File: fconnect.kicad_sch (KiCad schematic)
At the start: 201 parts, among them J1 9001-11961C00A, J2 9001-11961C00A, J3 7760, J4 7760

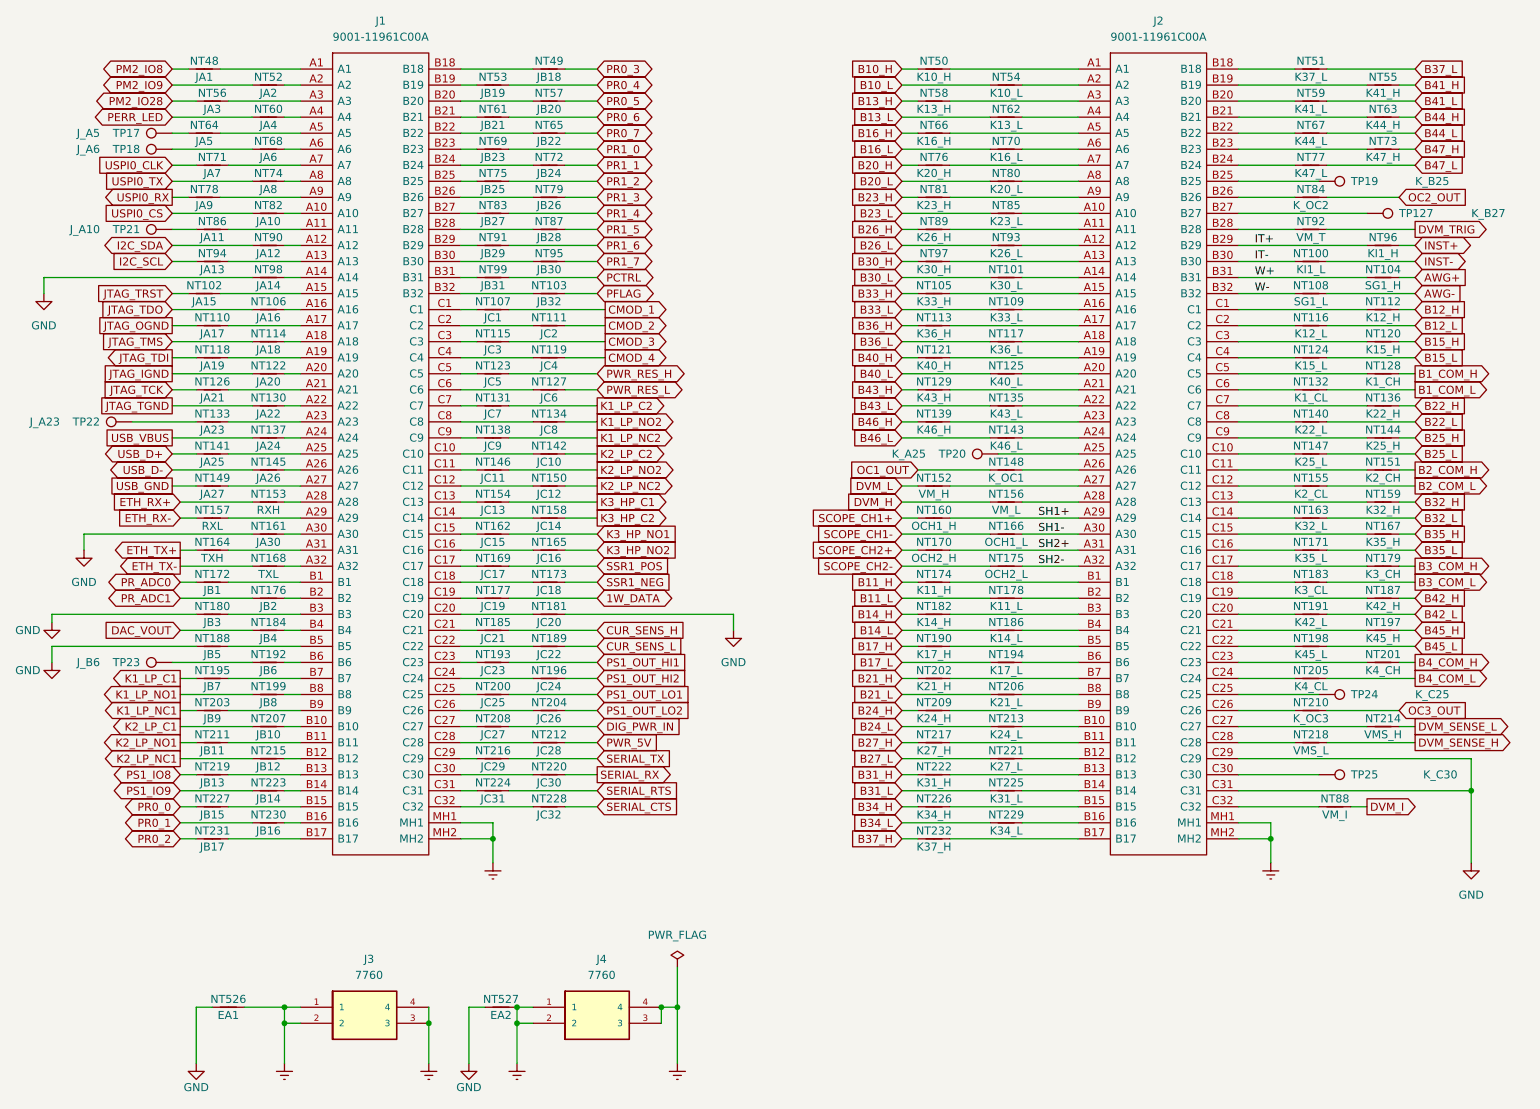
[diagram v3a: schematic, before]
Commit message: PCB Completed
PCB completed but final verification not completed
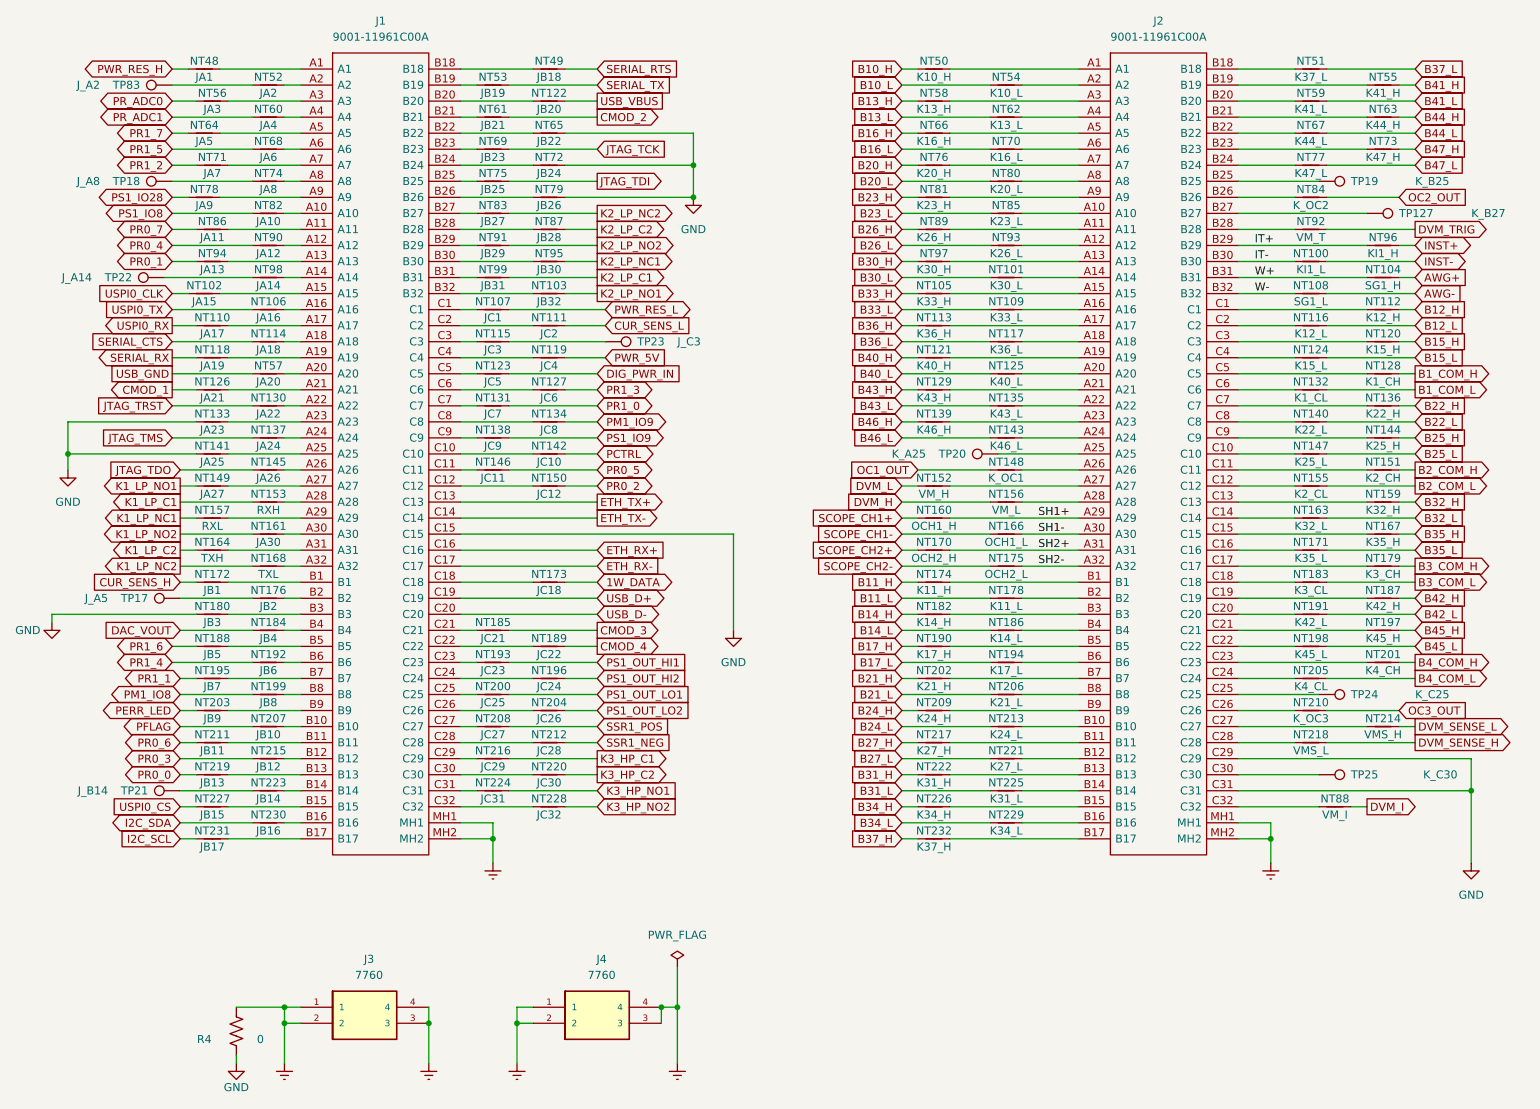
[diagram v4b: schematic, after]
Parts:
- removed NT154: JC13, NetTie:NetTie-2_Front1.0mm, symbol Device:NetTie_2
- removed NT158: JC14, NetTie:NetTie-2_Front1.0mm, symbol Device:NetTie_2
- removed NT162: JC15, NetTie:NetTie-2_Front1.0mm, symbol Device:NetTie_2
- removed NT165: JC16, NetTie:NetTie-2_Front1.0mm, symbol Device:NetTie_2
- removed NT169: JC17, NetTie:NetTie-2_Front1.0mm, symbol Device:NetTie_2
- removed NT177: JC19, NetTie:NetTie-2_Front1.0mm, symbol Device:NetTie_2
- removed NT181: JC20, NetTie:NetTie-2_Front1.0mm, symbol Device:NetTie_2
- removed NT526: EA1, NetTie:NetTie-2_Front1.0mm, symbol Device:NetTie_2
- removed NT527: EA2, NetTie:NetTie-2_Front1.0mm, symbol Device:NetTie_2
- added R4: 0, Resistor_THT:R_Axial_DIN0309_L9.0mm_D3.2mm_P12.70mm_Horizontal, symbol Device:R_US
- added TP83: J_A2, TestPoint:TestPoint_THTPad_D1.5mm_Drill0.7mm, symbol Connector:TestPoint
- NT122: value JA20 -> JB20
- NT57: value JB20 -> JA20
- TP17: footprint Connector_Pin:Pin_D0.9mm_L10.0mm_W2.4mm_FlatFork -> TestPoint:TestPoint_THTPad_D1.5mm_Drill0.7mm
- TP18: value J_A6 -> J_A8; footprint Connector_Pin:Pin_D0.9mm_L10.0mm_W2.4mm_FlatFork -> TestPoint:TestPoint_THTPad_D1.5mm_Drill0.7mm
- TP21: value J_A10 -> J_B14; footprint Connector_Pin:Pin_D0.9mm_L10.0mm_W2.4mm_FlatFork -> TestPoint:TestPoint_THTPad_D1.5mm_Drill0.7mm
- TP22: value J_A23 -> J_A14; footprint Connector_Pin:Pin_D0.9mm_L10.0mm_W2.4mm_FlatFork -> TestPoint:TestPoint_THTPad_D1.5mm_Drill0.7mm
- TP23: value J_B6 -> J_C3; footprint Connector_Pin:Pin_D0.9mm_L10.0mm_W2.4mm_FlatFork -> TestPoint:TestPoint_THTPad_D1.5mm_Drill0.7mm
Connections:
- net JTAG_IGND is gone; now on net USB_VBUS: NT122.1
- net JTAG_OGND is gone; now on net USPI0_RX: NT110.1
- net JTAG_TGND is gone; now on net JTAG_TRST: NT130.1
- net PM2_IO28 is gone; now on net PR_ADC0: NT56.1
- net PM2_IO8 is gone; now on net PWR_RES_H: NT48.1
- net 1W_DATA: now also NT173.1
- net CMOD_1: now also NT126.1; no longer NT107.1
- net CMOD_2: now also NT61.1; no longer NT111.1
- net CMOD_3: now also NT185.1; no longer NT115.1
- net CMOD_4: now also NT189.1; no longer NT119.1
- net CUR_SENS_H: now also NT172.1; no longer NT185.1
- net CUR_SENS_L: now also NT111.1; no longer NT189.1
- net DIG_PWR_IN: now also NT123.1; no longer NT208.1
- net ETH_RX+: now also J1.C16; no longer NT153.1
- net ETH_RX-: now also J1.C17; no longer NT157.1
- net ETH_TX+: now also J1.C13; no longer NT164.1
- net ETH_TX-: now also J1.C14; no longer NT168.1
- net Earth: now also R4.2
- net GND: now also J1.C15, NT133.1, NT141.1, NT65.1, NT72.1, NT79.1, R4.1; no longer NT161.1, NT188.1, NT98.1
- net I2C_SCL: now also NT231.1; no longer NT94.1
- net I2C_SDA: now also NT230.1; no longer NT90.1
- net JTAG_TCK: now also NT69.1; no longer NT126.1
- net JTAG_TDI: now also NT75.1; no longer NT118.1
- net JTAG_TDO: now also NT145.1; no longer NT106.1
- net JTAG_TMS: now also NT137.1; no longer NT114.1
- net JTAG_TRST: no longer NT102.1
- net K1_LP_C1: now also NT153.1; no longer NT195.1
- net K1_LP_C2: now also NT164.1; no longer NT131.1
- net K1_LP_NC1: now also NT157.1; no longer NT203.1
- net K1_LP_NC2: now also NT168.1; no longer NT138.1
- net K1_LP_NO1: now also NT149.1; no longer NT199.1
- net K1_LP_NO2: now also NT161.1; no longer NT134.1
- net K2_LP_C1: now also NT99.1; no longer NT207.1
- net K2_LP_C2: now also NT87.1; no longer NT142.1
- net K2_LP_NC1: now also NT95.1; no longer NT215.1
- net K2_LP_NC2: now also NT83.1; no longer NT150.1
- net K2_LP_NO1: now also NT103.1; no longer NT211.1
- net K2_LP_NO2: now also NT91.1; no longer NT146.1
- net K3_HP_C1: now also NT216.1
- net K3_HP_C2: now also NT220.1
- net K3_HP_NO1: now also NT224.1
- net K3_HP_NO2: now also NT228.1
- net PCTRL: now also NT142.1; no longer NT99.1
- net PERR_LED: now also NT203.1; no longer NT60.1
- net PFLAG: now also NT207.1; no longer NT103.1
- net PR0_0: now also NT219.1; no longer NT227.1
- net PR0_1: now also NT94.1; no longer NT230.1
- net PR0_2: now also NT150.1; no longer NT231.1
- net PR0_3: now also NT215.1; no longer NT49.1
- net PR0_4: now also NT90.1; no longer NT53.1
- net PR0_5: now also NT146.1; no longer NT57.1
- net PR0_6: now also NT211.1; no longer NT61.1
- net PR0_7: now also NT86.1; no longer NT65.1
- net PR1_0: now also NT131.1; no longer NT69.1
- net PR1_1: now also NT195.1; no longer NT72.1
- net PR1_2: now also NT71.1; no longer NT75.1
- net PR1_3: now also NT127.1; no longer NT79.1
- net PR1_4: now also NT192.1; no longer NT83.1
- net PR1_5: now also NT68.1; no longer NT87.1
- net PR1_6: now also NT188.1; no longer NT91.1
- net PR1_7: now also NT64.1; no longer NT95.1
- net PR_ADC0: no longer NT172.1
- net PR_ADC1: now also NT60.1; no longer NT176.1
- net PS1_IO8: now also NT82.1; no longer NT219.1
- net PS1_IO9: now also NT138.1; no longer NT223.1
- net PWR_5V: now also NT119.1; no longer NT212.1
- net PWR_RES_H: no longer NT123.1
- net PWR_RES_L: now also NT107.1; no longer NT127.1
- net SERIAL_CTS: now also NT114.1; no longer NT228.1
- net SERIAL_RTS: now also NT49.1; no longer NT224.1
- net SERIAL_RX: now also NT118.1; no longer NT220.1
- net SERIAL_TX: now also NT53.1; no longer NT216.1
- net SSR1_NEG: now also NT212.1; no longer NT173.1
- net SSR1_POS: now also NT208.1
- net USB_D+: now also J1.C19; no longer NT141.1
- net USB_D-: now also J1.C20; no longer NT145.1
- net USB_GND: now also NT57.1; no longer NT149.1
- net USB_VBUS: no longer NT137.1
- net USPI0_CLK: now also NT102.1; no longer NT71.1
- net USPI0_CS: now also NT227.1; no longer NT82.1
- net USPI0_RX: no longer NT78.1
- net USPI0_TX: now also NT106.1; no longer NT74.1
- net at TP21.1: now also NT223.1; no longer NT86.1
- net at TP17.1: now also NT176.1; no longer NT64.1
- net at TP22.1: now also NT98.1; no longer NT133.1
- net at TP18.1: now also NT74.1; no longer NT68.1
- net at NT122.2: now also J1.B20; no longer J1.A20
- net at NT57.2: now also J1.A20; no longer J1.B20
- net at TP23.1: now also NT115.1; no longer NT192.1
- net PM2_IO9: no longer names the net of NT52.1
- net PM2_IO9: now also TP83.1
- new net PM1_IO8: NT199.1
- new net PM1_IO9: NT134.1
- new net PS1_IO28: NT78.1
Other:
- moved on the sheet: TP21, TP22

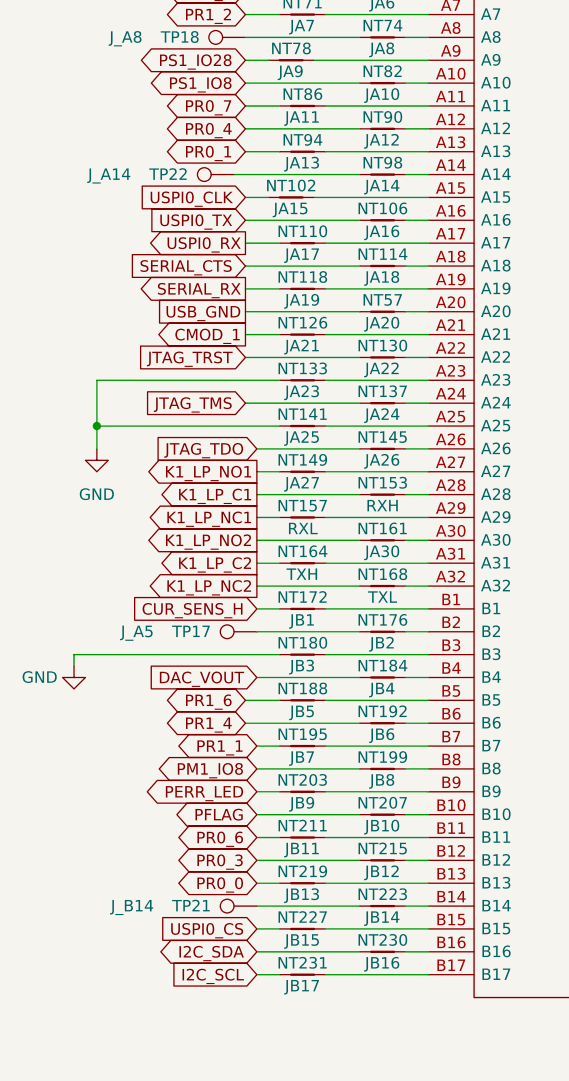
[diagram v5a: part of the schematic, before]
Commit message: Change custom connector
Use 8 pins to replace 6 pins
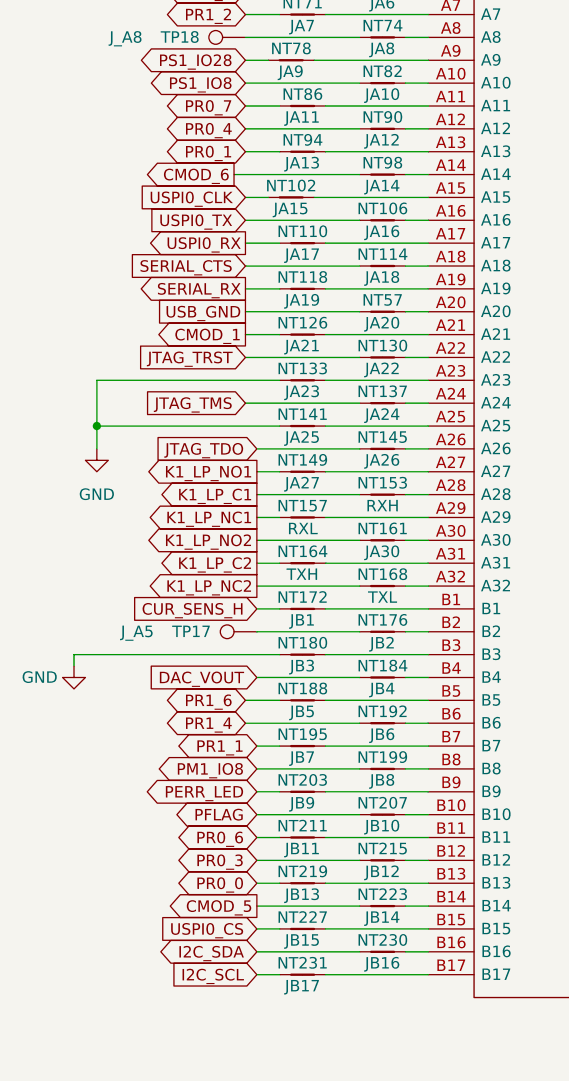
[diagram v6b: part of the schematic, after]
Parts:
- removed TP21: J_B14, TestPoint:TestPoint_THTPad_D1.5mm_Drill0.7mm, symbol Connector:TestPoint
- removed TP22: J_A14, TestPoint:TestPoint_THTPad_D1.5mm_Drill0.7mm, symbol Connector:TestPoint
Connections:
- net CMOD_5: now reaches NT223.1
- net CMOD_6: now reaches NT98.1
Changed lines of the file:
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@@
+    )
+  )
+  (global_label "CMOD_6" (shape output) (at 43.18 69.85 180) (fields_autoplaced)
+    (effects (font (size 1.27 1.27)) (justify right))
+    (property "Intersheet References" "${INTERSHEET_REFS}" (id 0) (at 33.2679 69.7706 0)
+      (effects (font (size 1.27 1.27)) (justify right) hide)
     )
   )
@@
     (property "Intersheet References" "${INTERSHEET_REFS}" (id 0) (at 249.5793 57.0706 0)
       (effects (font (size 1.27 1.27)) (justify left) hide)
+    )
+  )
+  (global_label "CMOD_5" (shape output) (at 45.72 151.13 180) (fields_autoplaced)
+    (effects (font (size 1.27 1.27)) (justify right))
+    (property "Intersheet References" "${INTERSHEET_REFS}" (id 0) (at 35.8079 151.0506 0)
+      (effects (font (size 1.27 1.27)) (justify right) hide)
     )
   )
@@
     (pin "2")
   )
-  (symbol (lib_id "Connector:TestPoint") (at 45.72 151.13 90) (mirror x) (unit 1)
-    (in_bom yes) (on_board yes)
-    (property "Reference" "TP21" (id 0) (at 40.64 151.13 90)
-      (effects (font (size 1.27 1.27)) (justify left))
-    )
-    (property "Value" "J_B14" (id 1) (at 34.29 151.13 90)
-      (effects (font (size 1.27 1.27)) (justify left))
-    )
-    (property "Footprint" "TestPoint:TestPoint_THTPad_D1.5mm_Drill0.7mm" (id 2) (at 45.72 156.21 0)
-      (effects (font (size 1.27 1.27)) hide)
-    )
-    (property "Datasheet" "~" (id 3) (at 45.72 156.21 0)
-      (effects (font (size 1.27 1.27)) hide)
-    )
-    (pin "1")
-  )
   (symbol (lib_id "Device:NetTie_2") (at 95.25 130.81 0) (mirror y) (unit 1)
     (in_bom yes) (on_board yes)
@@
       (effects (font (size 1.27 1.27)) hide)
     )
-    (pin "1")
-  )
-  (symbol (lib_id "Connector:TestPoint") (at 43.18 69.85 90) (mirror x) (unit 1)
-    (in_bom yes) (on_board yes)
-    (property "Reference" "TP22" (id 0) (at 38.1 69.85 90)
-      (effects (font (size 1.27 1.27)) (justify left))
-    )
-    (property "Value" "J_A14" (id 1) (at 31.75 69.85 90)
-      (effects (font (size 1.27 1.27)) (justify left))
-    )
-    (property "Footprint" "TestPoint:TestPoint_THTPad_D1.5mm_Drill0.7mm" (id 2) (at 43.18 74.93 0)
-      (effects (font (size 1.27 1.27)) hide)
-    )
-    (property "Datasheet" "~" (id 3) (at 43.18 74.93 0)
-      (effects (font (size 1.27 1.27)) hide)
-    )

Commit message: update
Correction of small error
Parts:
- R4: footprint Resistor_THT:R_Axial_DIN0309_L9.0mm_D3.2mm_P12.70mm_Horizontal -> Resistor_THT:R_Axial_DIN0207_L6.3mm_D2.5mm_P10.16mm_Horizontal
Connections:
- net CUR_SENS_H: now also NT107.1; no longer NT172.1
- net PWR_RES_L: now also NT172.1; no longer NT107.1
- net PS1_IO28 renamed DIG_SPARE
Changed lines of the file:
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@@
     )
   )
-  (global_label "PS1_IO28" (shape bidirectional) (at 44.45 57.15 180) (fields_autoplaced)
-    (effects (font (size 1.27 1.27)) (justify right))
-    (property "Intersheet References" "${INTERSHEET_REFS}" (id 0) (at 33.0259 57.0706 0)
+  (global_label "DIG_SPARE" (shape bidirectional) (at 44.45 57.15 180) (fields_autoplaced)
+    (effects (font (size 1.27 1.27)) (justify right))
+    (property "Intersheet References" "${INTERSHEET_REFS}" (id 0) (at 31.9374 57.0706 0)
       (effects (font (size 1.27 1.27)) (justify right) hide)
     )
@@
     )
   )
-  (global_label "CUR_SENS_H" (shape input) (at 45.72 118.11 180) (fields_autoplaced)
-    (effects (font (size 1.27 1.27)) (justify right))
-    (property "Intersheet References" "${INTERSHEET_REFS}" (id 0) (at 31.2721 118.0306 0)
-      (effects (font (size 1.27 1.27)) (justify right) hide)
-    )
-  )
   (global_label "PR0_4" (shape bidirectional) (at 44.45 64.77 180) (fields_autoplaced)
     (effects (font (size 1.27 1.27)) (justify right))
@@
     )
   )
-  (global_label "PWR_RES_L" (shape bidirectional) (at 113.03 74.93 0) (fields_autoplaced)
-    (effects (font (size 1.27 1.27)) (justify left))
-    (property "Intersheet References" "${INTERSHEET_REFS}" (id 0) (at 126.0264 74.8506 0)
-      (effects (font (size 1.27 1.27)) (justify left) hide)
-    )
-  )
   (global_label "B33_H" (shape input) (at 160.02 72.39 180) (fields_autoplaced)
     (effects (font (size 1.27 1.27)) (justify right))
@@
     )
   )
+  (global_label "CUR_SENS_H" (shape input) (at 113.03 74.93 0) (fields_autoplaced)
+    (effects (font (size 1.27 1.27)) (justify left))
+    (property "Intersheet References" "${INTERSHEET_REFS}" (id 0) (at 127.4779 74.8506 0)
+      (effects (font (size 1.27 1.27)) (justify left) hide)
+    )
+  )
   (global_label "K1_LP_C2" (shape output) (at 45.72 113.03 180) (fields_autoplaced)
     (effects (font (size 1.27 1.27)) (justify right))
@@
     (property "Intersheet References" "${INTERSHEET_REFS}" (id 0) (at 123.8493 41.9894 0)
       (effects (font (size 1.27 1.27)) (justify left) hide)
+    )
+  )
+  (global_label "PWR_RES_L" (shape bidirectional) (at 45.72 118.11 180) (fields_autoplaced)
+    (effects (font (size 1.27 1.27)) (justify right))
+    (property "Intersheet References" "${INTERSHEET_REFS}" (id 0) (at 32.7236 118.0306 0)
+      (effects (font (size 1.27 1.27)) (justify right) hide)
     )
   )
@@
     (property "Reference" "R4" (id 0) (at 49.53 190.5 0))
     (property "Value" "0" (id 1) (at 58.42 190.5 0))
-    (property "Footprint" "Resistor_THT:R_Axial_DIN0309_L9.0mm_D3.2mm_P12.70mm_Horizontal" (id 2) (at 53.594 188.976 90)
-      (effects (font (size 1.27 1.27)) hide)
-    )
+    (property "Footprint" "Resistor_THT:R_Axial_DIN0207_L6.3mm_D2.5mm_P10.16mm_Horizontal" (id 2) (at 53.594 188.976 90)
+      (effects (font (size 1.27 1.27)) hide)
+    )
